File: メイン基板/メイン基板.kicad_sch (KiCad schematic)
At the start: 21 parts, among them J1 Conn_01x02, J2 Conn_01x02, J3 Conn_01x02, J4 Conn_01x02, U1 Teensy4.1, U2 SN74LVC2G241DCUR, U3 VL5, U4 VL1, U5 VL1, U6 VL0, U7 VL0

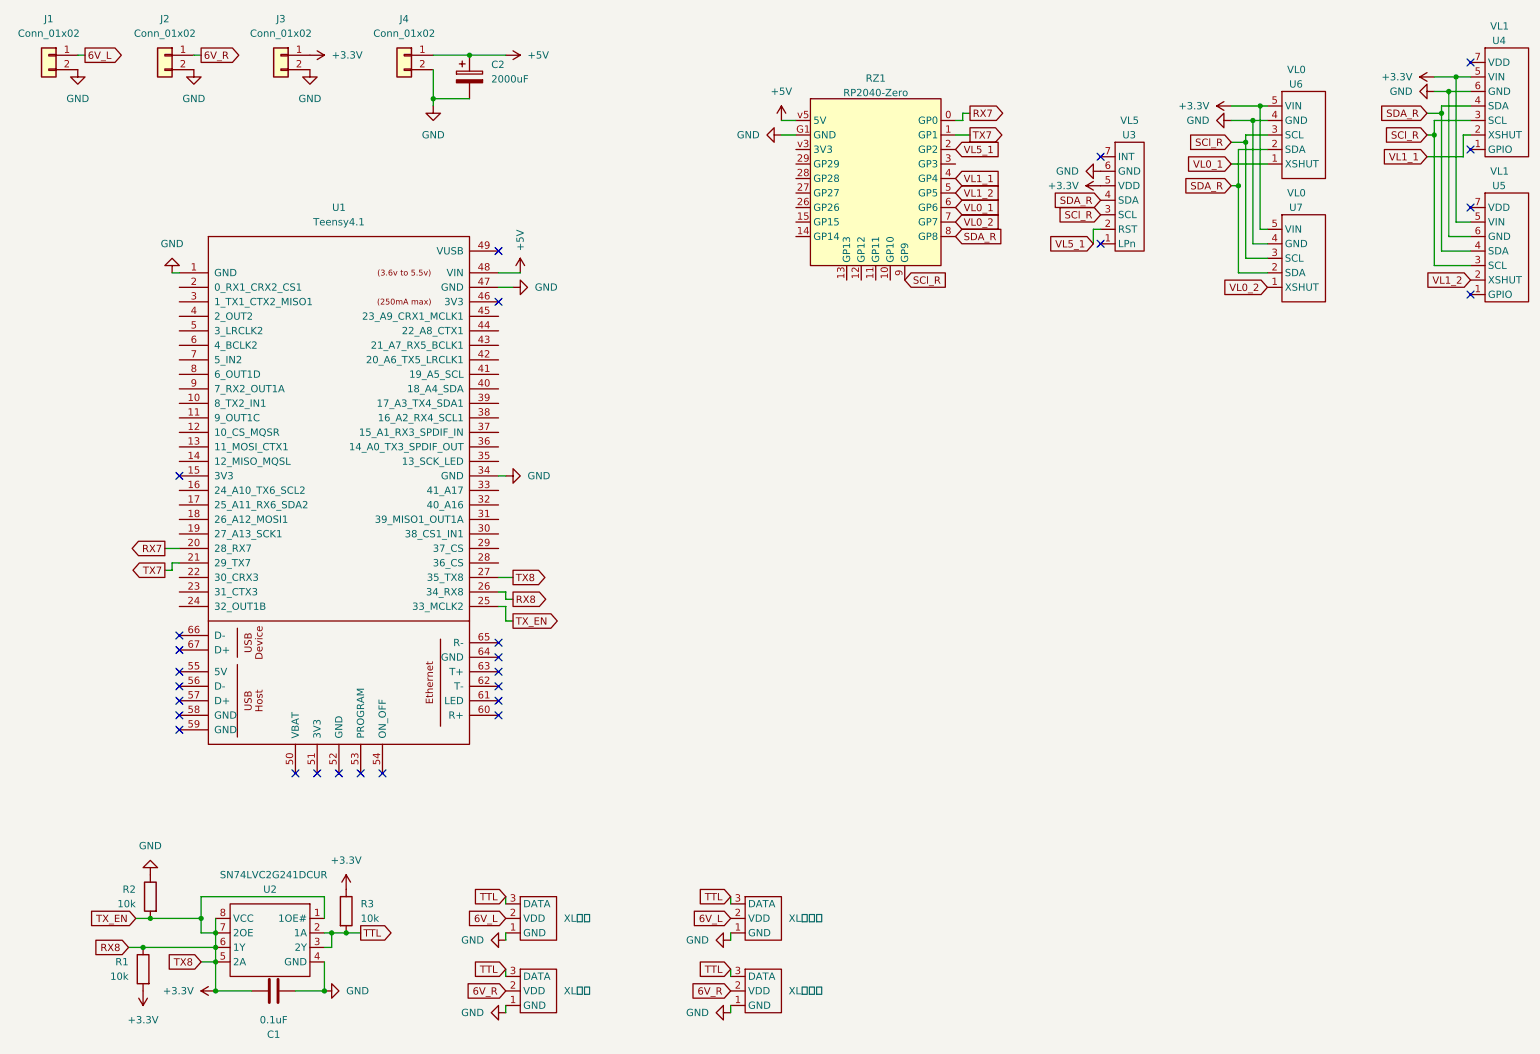
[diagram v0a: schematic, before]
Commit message: メイン基板 ジャイロ追加
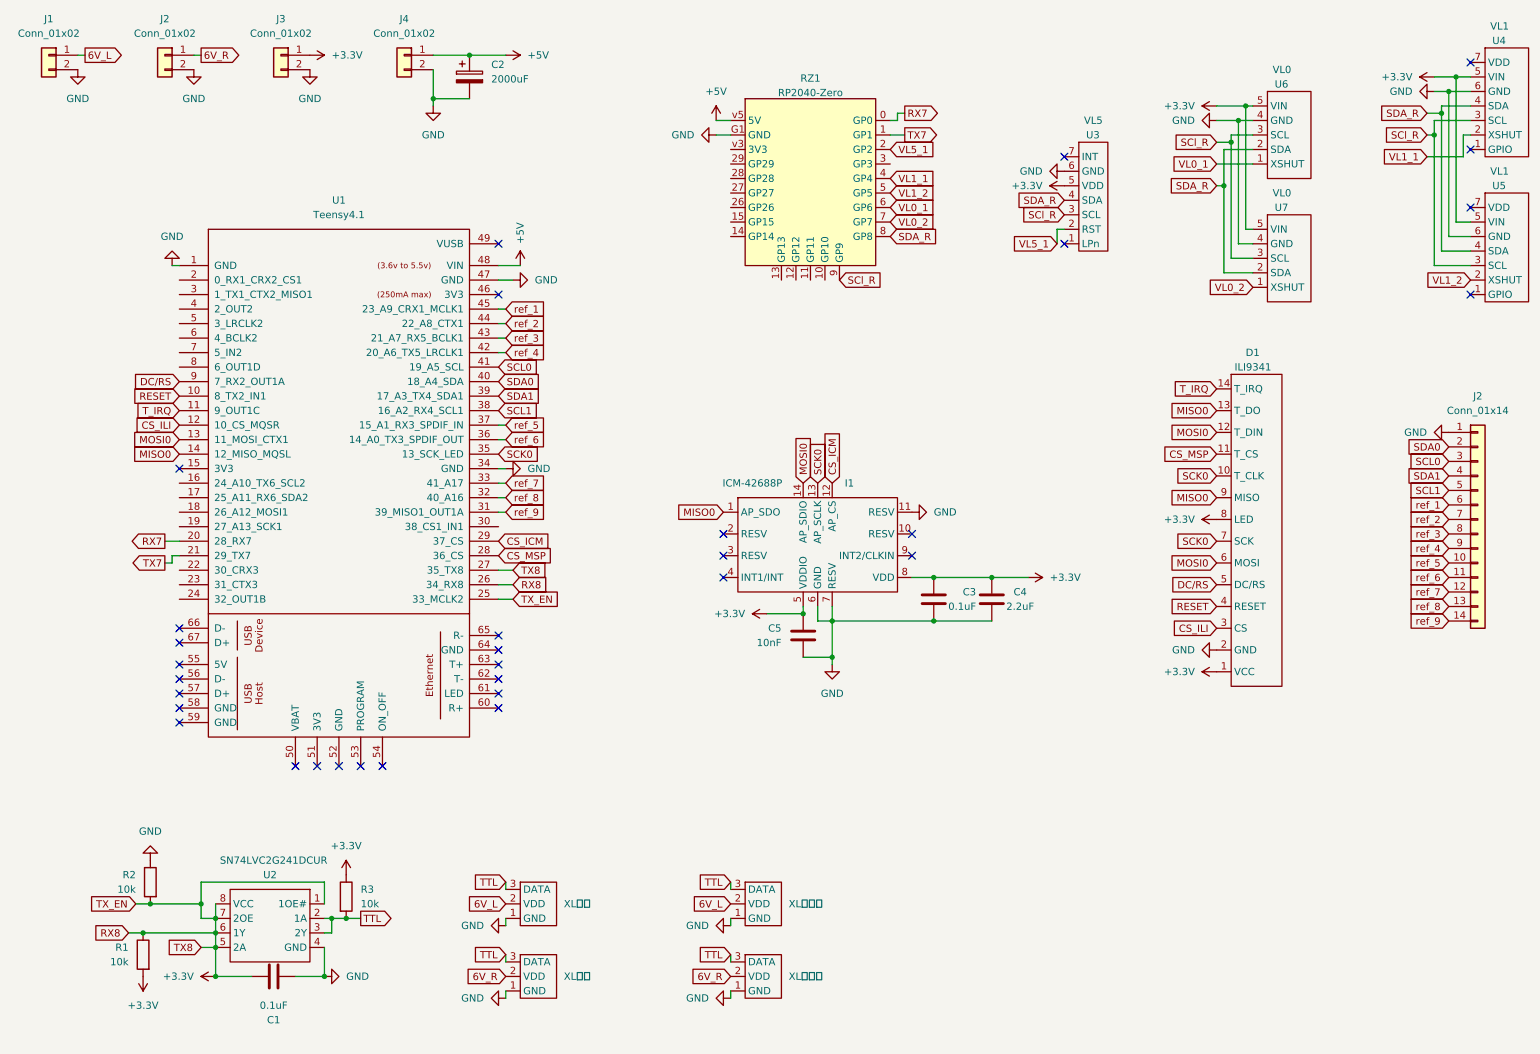
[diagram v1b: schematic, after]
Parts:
- added C3: 0.1uF, symbol Device:C
- added C4: 2.2uF, symbol Device:C
- added C5: 10nF, symbol Device:C
- added D1: ILI9341, symbol koki:ILI9341
- added I1: ICM-42688P, symbol koki:ICM42688p
- added J2: Conn_01x14, symbol Connector_Generic:Conn_01x14
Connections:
- net +3.3V: now also C3.1, C4.1, C5.1, D1.1 (VCC), D1.8 (LED), I1.5 (VDDIO), I1.8 (VDD)
- net GND: now also C3.2, C4.2, C5.2, D1.2 (GND), I1.11 (RESV), I1.6 (GND), I1.7 (RESV), J2.1 (Pin_1)
- net RESET: now reaches U1.10 (8_TX2_IN1)
- net RESET: now also D1.4 (RESET)
- net T_IRQ: now reaches U1.11 (9_OUT1C)
- net T_IRQ: now also D1.14 (T_IRQ)
- net CS_ILI: now reaches U1.12 (10_CS_MQSR)
- net CS_ILI: now also D1.3 (CS)
- net MOSI0: now reaches U1.13 (11_MOSI_CTX1)
- net MOSI0: now also D1.12 (T_DIN), D1.6 (MOSI), I1.14 (AP_SDIO)
- net MISO0: now reaches U1.14 (12_MISO_MQSL)
- net MISO0: now also D1.13 (T_DO), D1.9 (MISO), I1.1 (AP_SDO)
- net CS_MSP: now reaches U1.28 (36_CS)
- net CS_MSP: now also D1.11 (T_CS)
- net CS_ICM: now reaches U1.29 (37_CS)
- net CS_ICM: now also I1.12 (AP_CS)
- net ref_9: now reaches U1.31 (39_MISO1_OUT1A)
- net ref_9: now also J2.14 (Pin_14)
- net ref_8: now reaches U1.32 (40_A16)
- net ref_8: now also J2.13 (Pin_13)
- net ref_7: now reaches U1.33 (41_A17)
- net ref_7: now also J2.12 (Pin_12)
- net SCK0: now reaches U1.35 (13_SCK_LED)
- net SCK0: now also D1.10 (T_CLK), D1.7 (SCK), I1.13 (AP_SCLK)
- net ref_6: now reaches U1.36 (14_A0_TX3_SPDIF_OUT)
- net ref_6: now also J2.11 (Pin_11)
- net ref_5: now reaches U1.37 (15_A1_RX3_SPDIF_IN)
- net ref_5: now also J2.10 (Pin_10)
- net SCL1: now reaches U1.38 (16_A2_RX4_SCL1)
- net SCL1: now also J2.5 (Pin_5)
- net SDA1: now reaches U1.39 (17_A3_TX4_SDA1)
- net SDA1: now also J2.4 (Pin_4)
- net SDA0: now reaches U1.40 (18_A4_SDA)
- net SDA0: now also J2.2 (Pin_2)
- net SCL0: now reaches U1.41 (19_A5_SCL)
- net SCL0: now also J2.3 (Pin_3)
- net ref_4: now reaches U1.42 (20_A6_TX5_LRCLK1)
- net ref_4: now also J2.9 (Pin_9)
- net ref_3: now reaches U1.43 (21_A7_RX5_BCLK1)
- net ref_3: now also J2.8 (Pin_8)
- net ref_2: now reaches U1.44 (22_A8_CTX1)
- net ref_2: now also J2.7 (Pin_7)
- net ref_1: now reaches U1.45 (23_A9_CRX1_MCLK1)
- net ref_1: now also J2.6 (Pin_6)
- net DC/RS: now reaches U1.9 (7_RX2_OUT1A)
- net DC/RS: now also D1.5 (DC/RS)
- no-connect marks 27 -> 32
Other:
- moved on the sheet: C1, R1, R2, R3, RZ1, U1, U2, U3, U6, U7, XL右前, XL右後ろ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
